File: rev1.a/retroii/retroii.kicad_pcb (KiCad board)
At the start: 4 copper layers, 362 x 215.9 mm, 294 parts, among them CON1 SD_Card_SPI, J1 VGA, J10 BARREL_JACK, J11 Conn_02x10, J12 Peripheral Slot 0, J13 74LS74, J14 Game_IO_Socket, J15 Peripheral Slot 4, J16 Peripheral Slot 1, J17 Peripheral Slot 5, J18 Peripheral Slot 2, J19 Peripheral Slot 6, J2 DB9_Female_Stacked, J20 Peripheral Slot 3, J21 Peripheral Slot 7, J22 Conn_01x09, J23 Conn_01x02, J24 Headphone, J3 DB15_Female_Stacked, J6 Edge mounted connector, J7 Cassette In, J8 Cassette Out, J9 Speaker Jack, K1 PS2_KEYBOARD, K13 LM741, P1 PROP_PLUG, P2 PROP_PLUG, Q4 MPSA13, Q5 2N3904, SW1 SW_PUSH_SAFE, SW2 SPST2, SW3 SAVE, SW4 LOAD, SW5 SW_PUSH_SAFE, SW6 RESET, SW7 MISC1, SW8 MISC2, U1 74LS00, U10 74LS08, U11 LM2576-12, U12 LM2576-5, U13 LM2576-12, U14 LM2576-3.3, U15 LM2576-5, U16 Prop_P8X32A, U17 24LC256_EEPROM, U18 74LS04, U3 74LS11, U4 Prop_P8X32A, U5 24LC256_EEPROM, U6 AT28C256_EEPROM, U8 IDT7008_Dual_Port_RAM, U9 74LS32, Y1 5MHz 20pf, Y2 ECS-2100X-1MHZ, Y3 5MHz 20pf

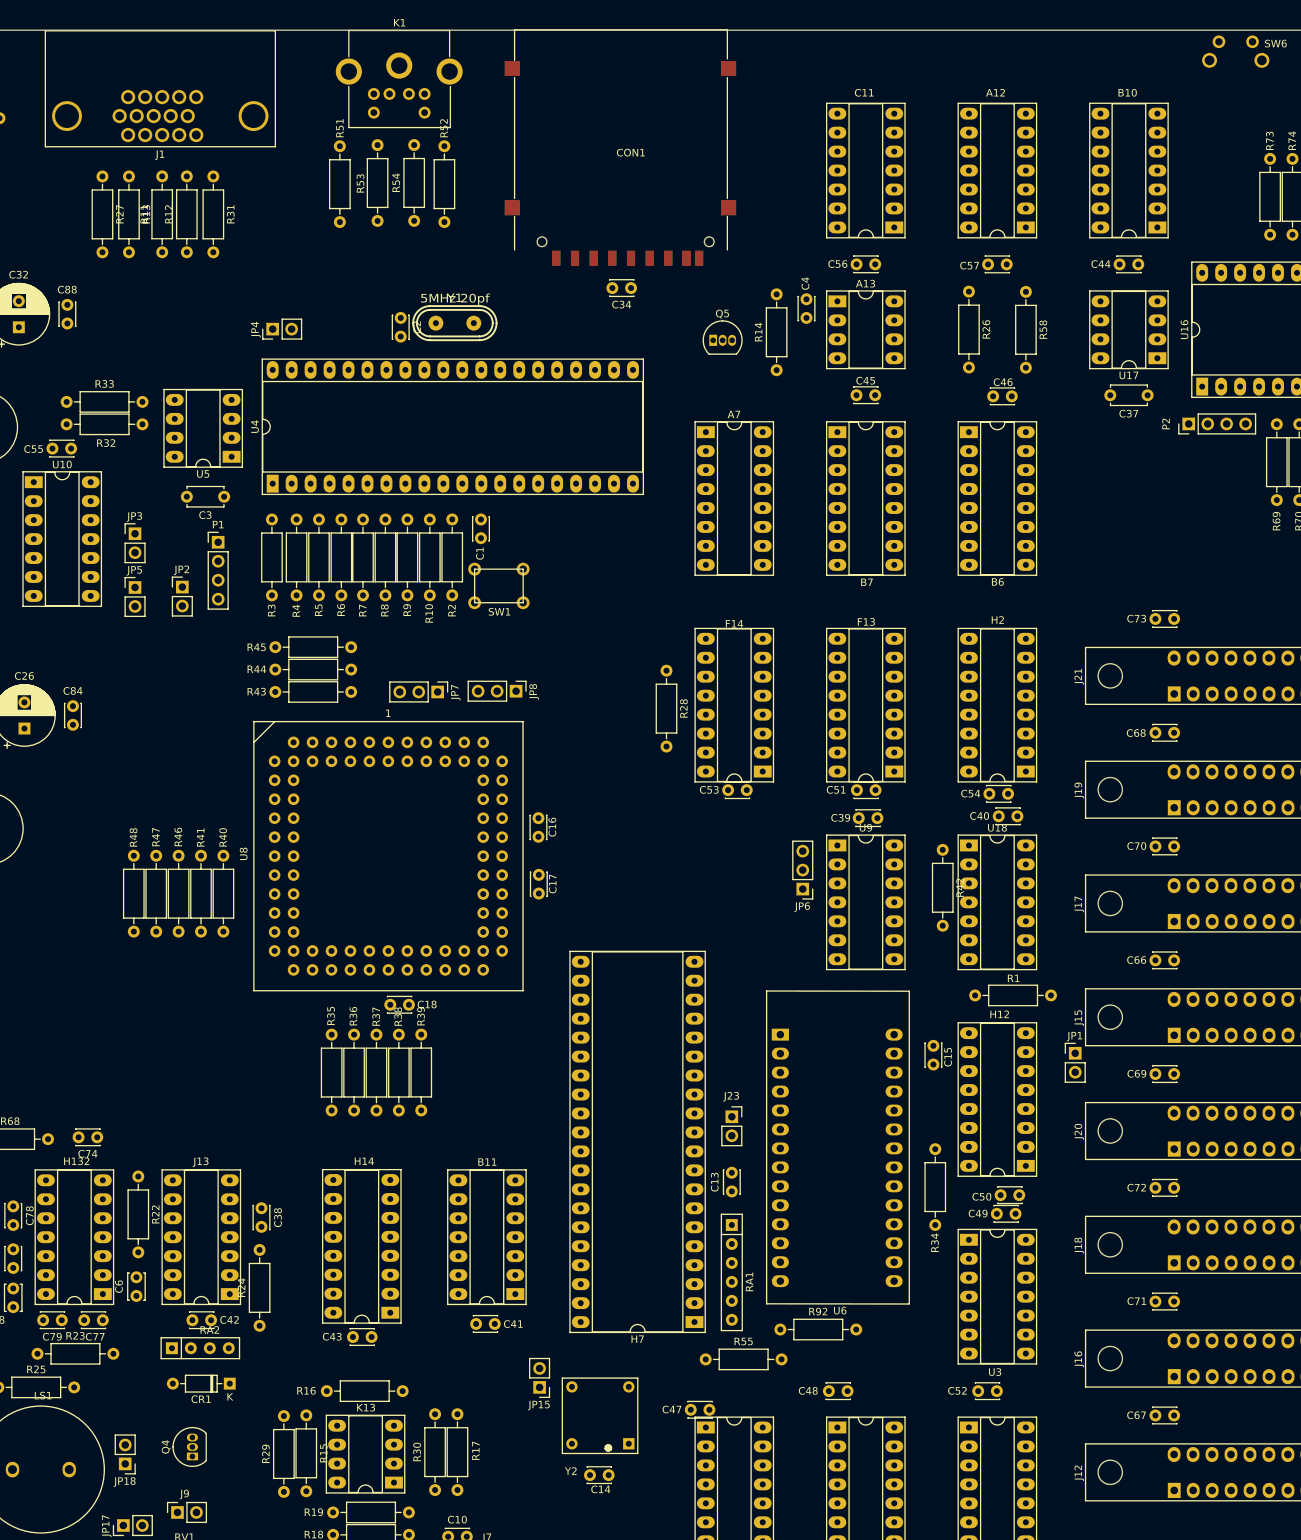
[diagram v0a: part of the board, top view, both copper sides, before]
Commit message: more keyboard circuit layout changes
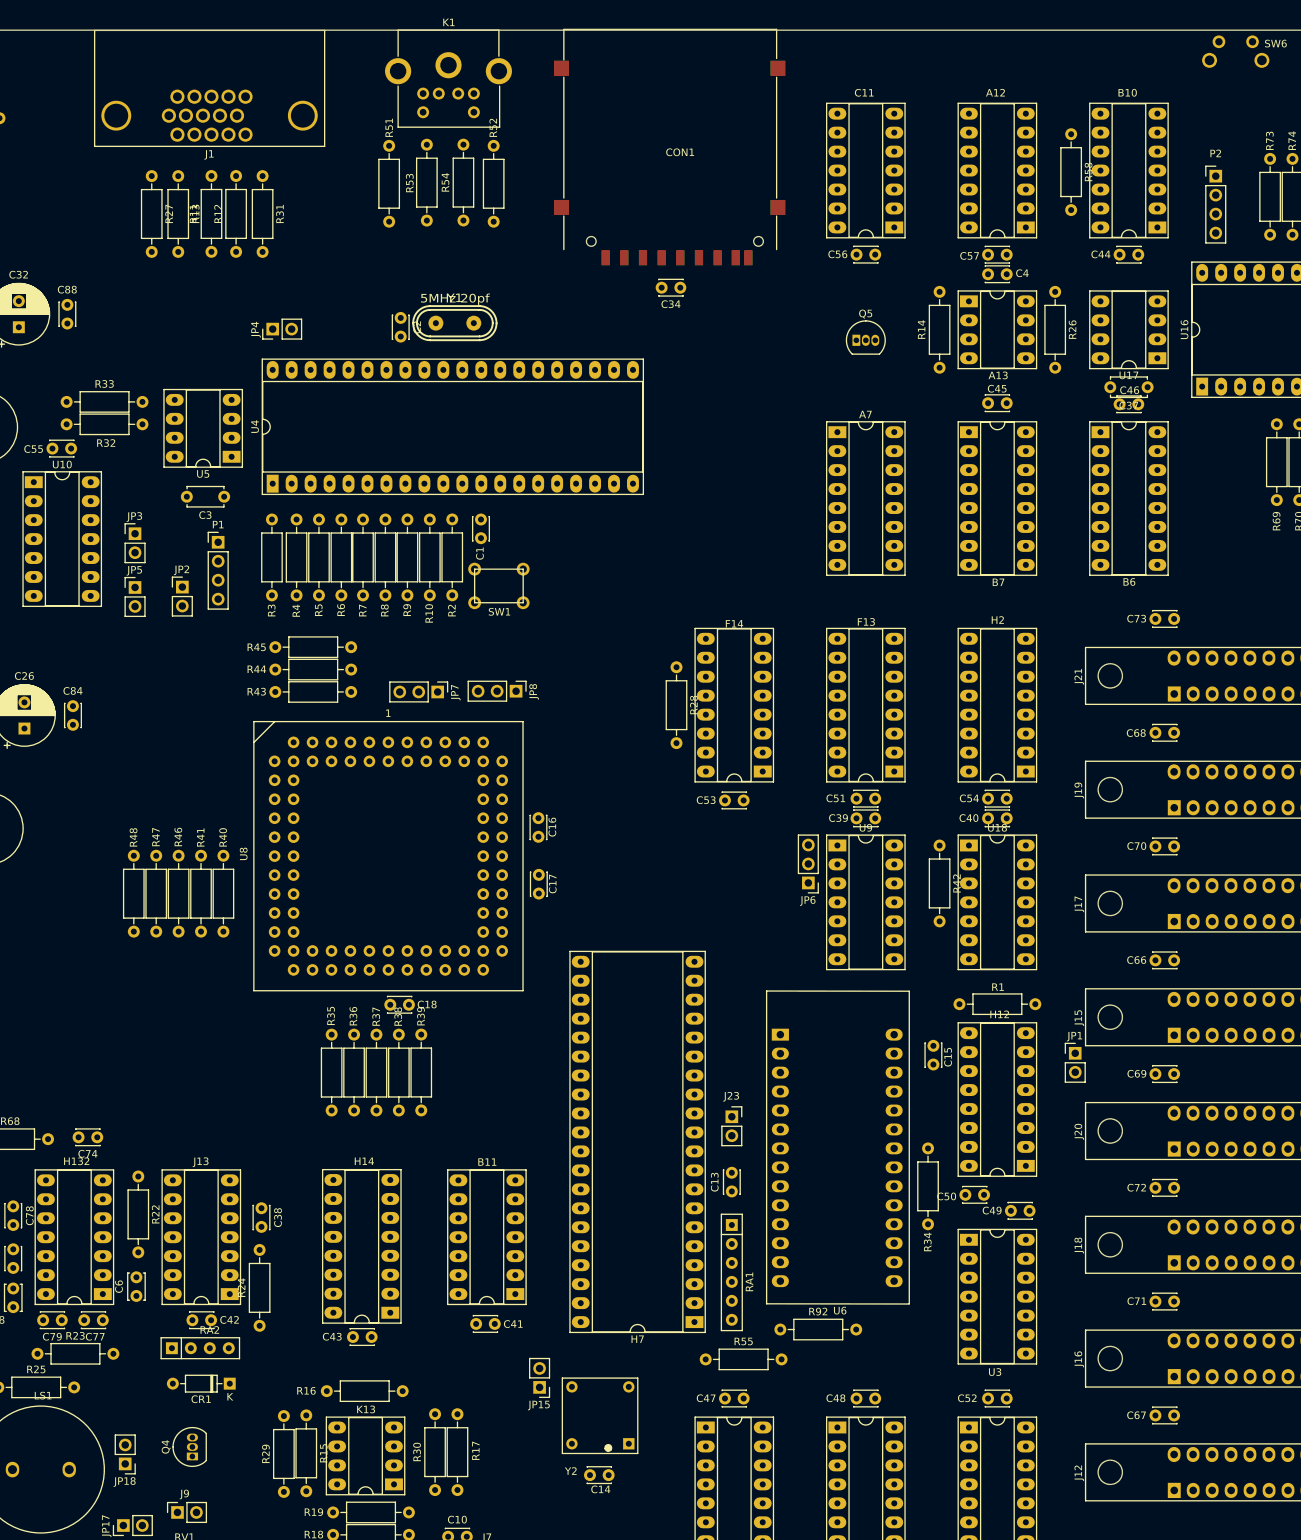
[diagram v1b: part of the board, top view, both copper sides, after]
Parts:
- moved P2 33.4 mm to (488.8, 169.5), turned to 0 degrees
- moved C4 25.0 mm to (458.3, 182.7), turned to 0 degrees
- moved R58 22.0 mm to (469.4, 163.9)
- moved R14 21.8 mm to (451.8, 195.2)
- moved Q5 19.2 mm to (440.7, 191.5)
- moved C45 17.7 mm to (460.8, 199.9)
- moved A13 17.6 mm to (455.8, 186.3)
- moved A7 17.6 mm to (438.1, 203.8)
- moved B6 17.6 mm to (473.4, 203.8)
- moved B7 17.6 mm to (455.8, 203.8)
- moved C46 17.0 mm to (478.4, 200.1)
- moved R26 11.6 mm to (467.3, 185.0)
- moved C34 6.60 mm to (417.1, 184.4)
- moved CON1 6.60 mm to (417.1, 180.4)
- moved J1 6.60 mm to (371.1, 158.4)
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
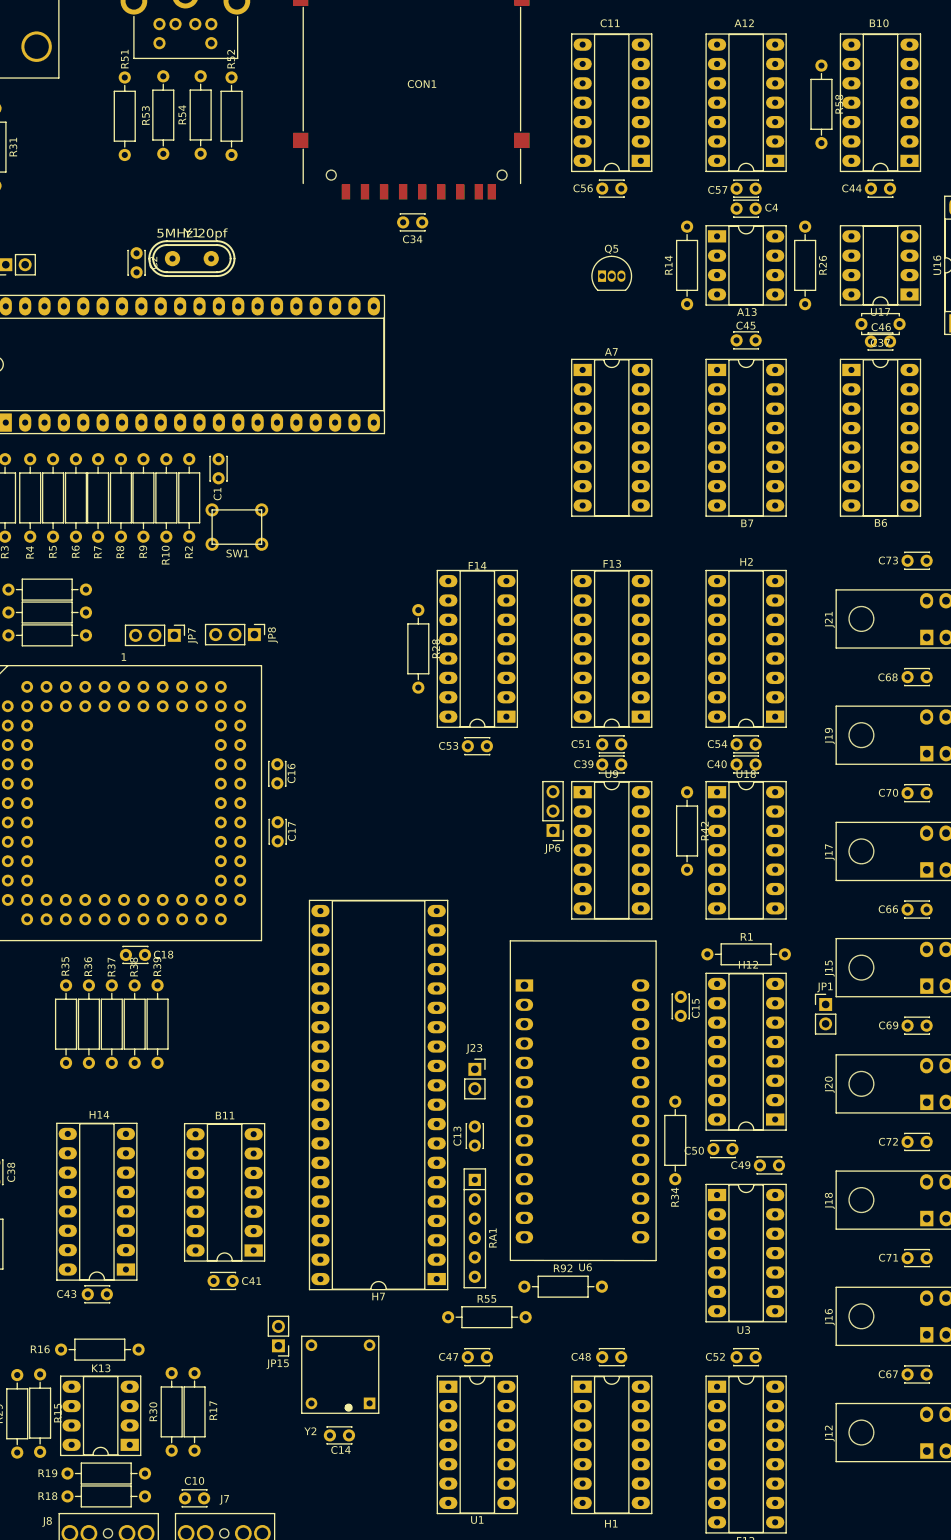
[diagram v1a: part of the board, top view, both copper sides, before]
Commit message: more general layout (address decoding, timing, keyboard)
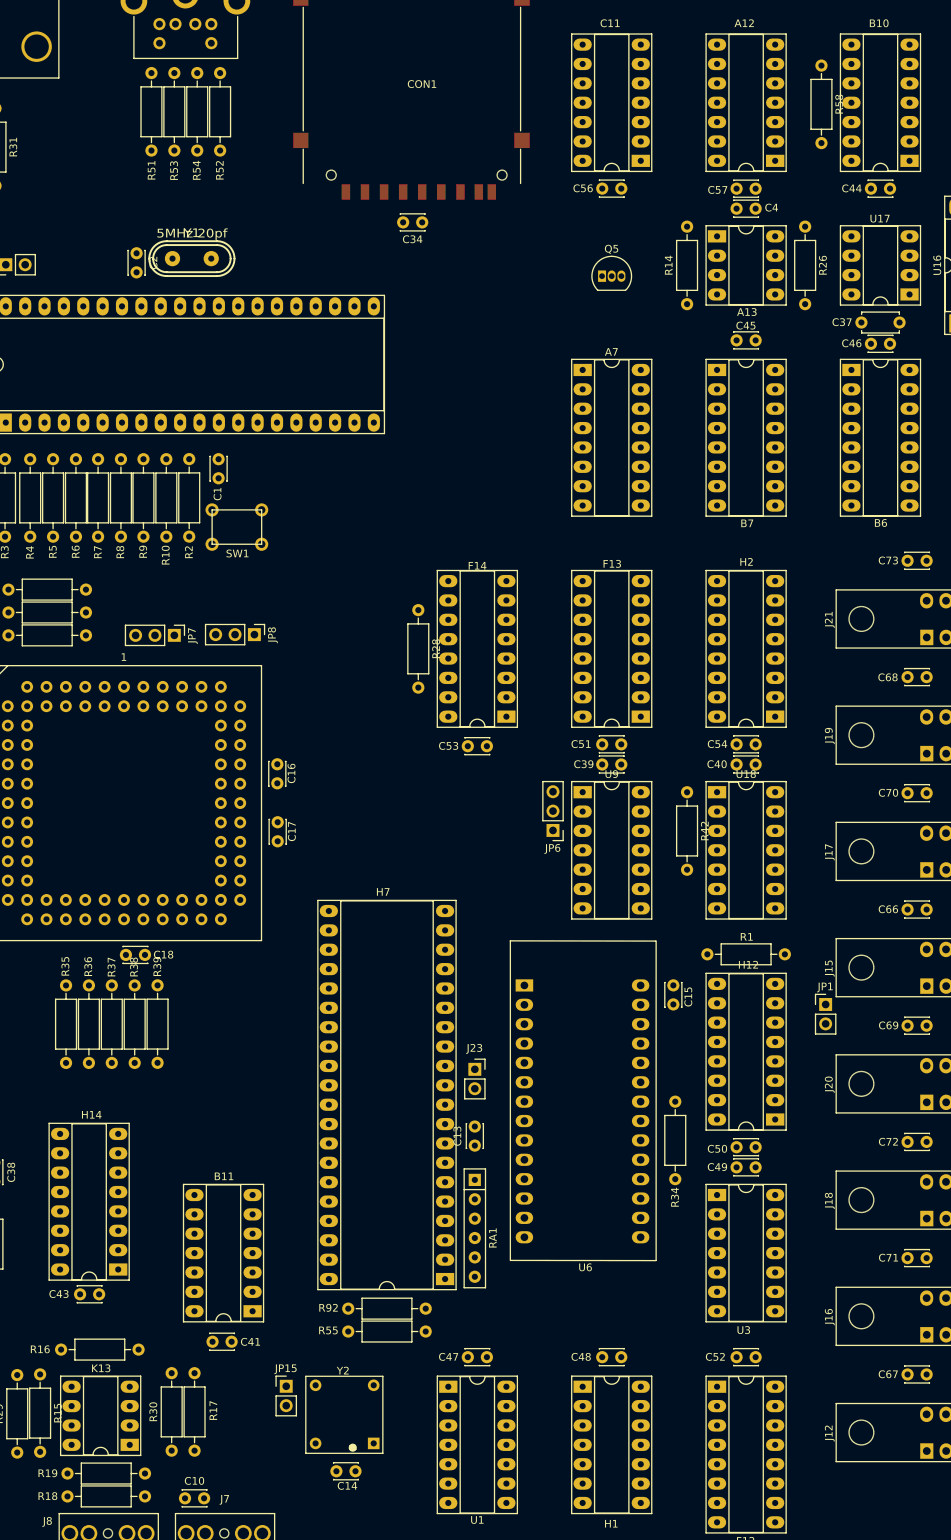
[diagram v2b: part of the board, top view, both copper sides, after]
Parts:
- moved R92 23.3 mm to (407.4, 326.9)
- moved B11 7.97 mm to (394.9, 327.2)
- moved C41 7.97 mm to (389.6, 331.2)
- moved JP15 5.41 mm to (399.3, 337.1), turned to 0 degrees
- moved Y2 5.28 mm to (407.0, 340.8)
- moved C14 4.78 mm to (405.9, 348.2)
- moved R51 3.55 mm to (381.6, 164.9)
- moved R55 3.49 mm to (417.6, 329.9), turned to 180 degrees
- moved C49 3.07 mm to (460.8, 308.4)
- moved C50 3.05 mm to (458.3, 305.7)
- moved C15 1.79 mm to (450.0, 287.0)
- moved R52 1.61 mm to (390.6, 164.9)
- moved R53 1.51 mm to (384.6, 164.9)
- moved H7 1.10 mm to (420.1, 323.0)
- moved C43 1.01 mm to (374.7, 325.0)
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
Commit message: laying out audio/serial io
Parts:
- moved R20 52.3 mm to (363.3, 311.4), turned to 270 degrees
- moved R21 52.2 mm to (346.9, 311.6), turned to 270 degrees
- moved C42 49.6 mm to (359.1, 372.1)
- moved CR1 49.6 mm to (361.6, 380.6)
- moved RA2 49.6 mm to (353.9, 375.8)
- moved R23 43.6 mm to (346.9, 286.6), turned to 270 degrees
- moved C8 42.0 mm to (363.2, 324.5), turned to 270 degrees
- moved C75 39.9 mm to (366.0, 326.9)
- moved C9 39.7 mm to (356.6, 330.9)
- moved C76 38.2 mm to (347.6, 325.3)
- moved C77 37.1 mm to (368.1, 302.1), turned to 90 degrees
- moved H131 36.6 mm to (359.0, 327.2)
- moved U10 34.0 mm to (359.0, 229.0), turned to 180 degrees
- moved C5 32.2 mm to (343.0, 328.0)
- moved C79 28.0 mm to (356.5, 305.7)
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
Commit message: more layout
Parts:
- moved RA2 70.3 mm to (369.2, 307.2)
- moved JP3 62.1 mm to (371.6, 183.9)
- moved P1 59.5 mm to (368.0, 178.8)
- moved R68 58.4 mm to (382.8, 286.2), turned to 270 degrees
- moved JP2 58.3 mm to (364.4, 186.4), turned to 180 degrees
- moved CR1 57.3 mm to (379.5, 326.1), turned to 90 degrees
- moved C74 53.5 mm to (382.8, 302.1), turned to 90 degrees
- moved C42 44.4 mm to (373.7, 330.1)
- moved JP5 36.9 mm to (375.9, 231.1)
- moved R33 13.3 mm to (347.2, 204.8), turned to 90 degrees
- moved J6 12.1 mm to (296.2, 311.9)
- moved J14 11.6 mm to (306.1, 312.0)
- moved R32 9.53 mm to (344.2, 204.8), turned to 90 degrees
- moved J11 8.87 mm to (315.5, 297.6)
- moved R35 5.10 mm to (366.8, 280.9)
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
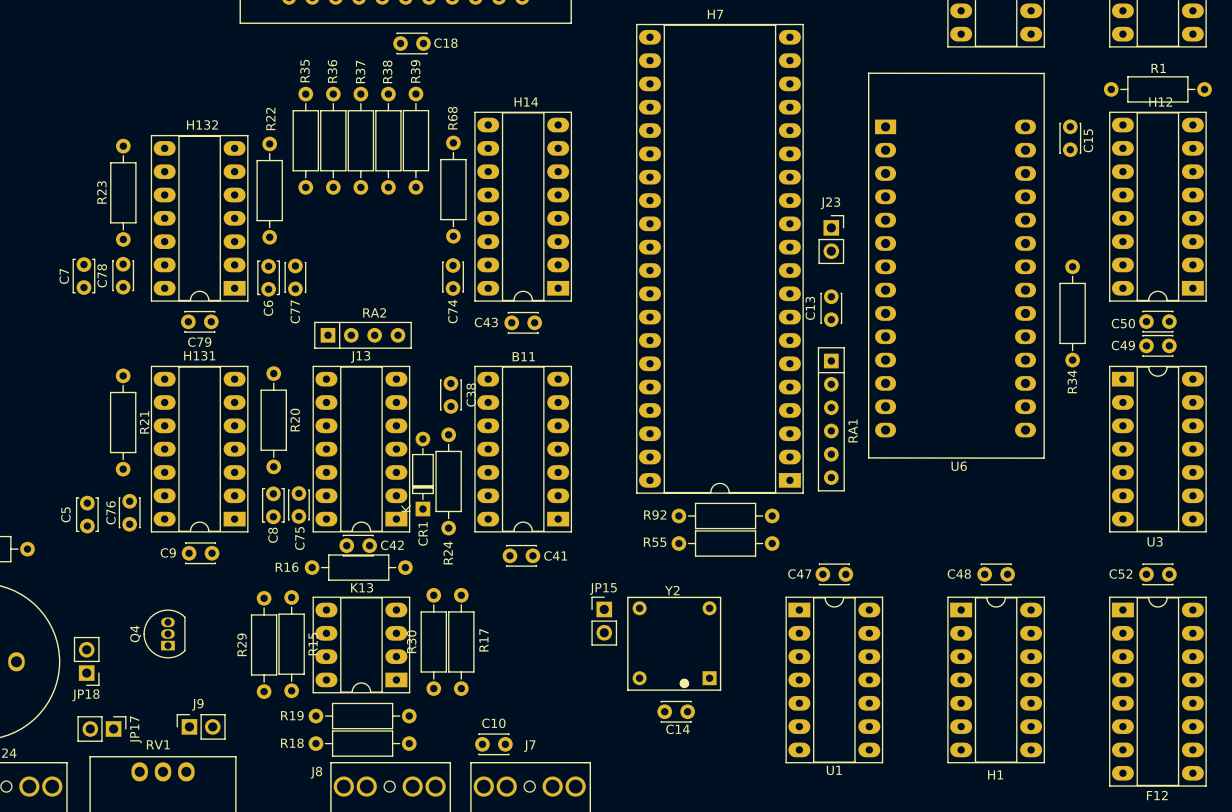
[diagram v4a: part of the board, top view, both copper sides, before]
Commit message: layout for audio/cassette in/out and serial
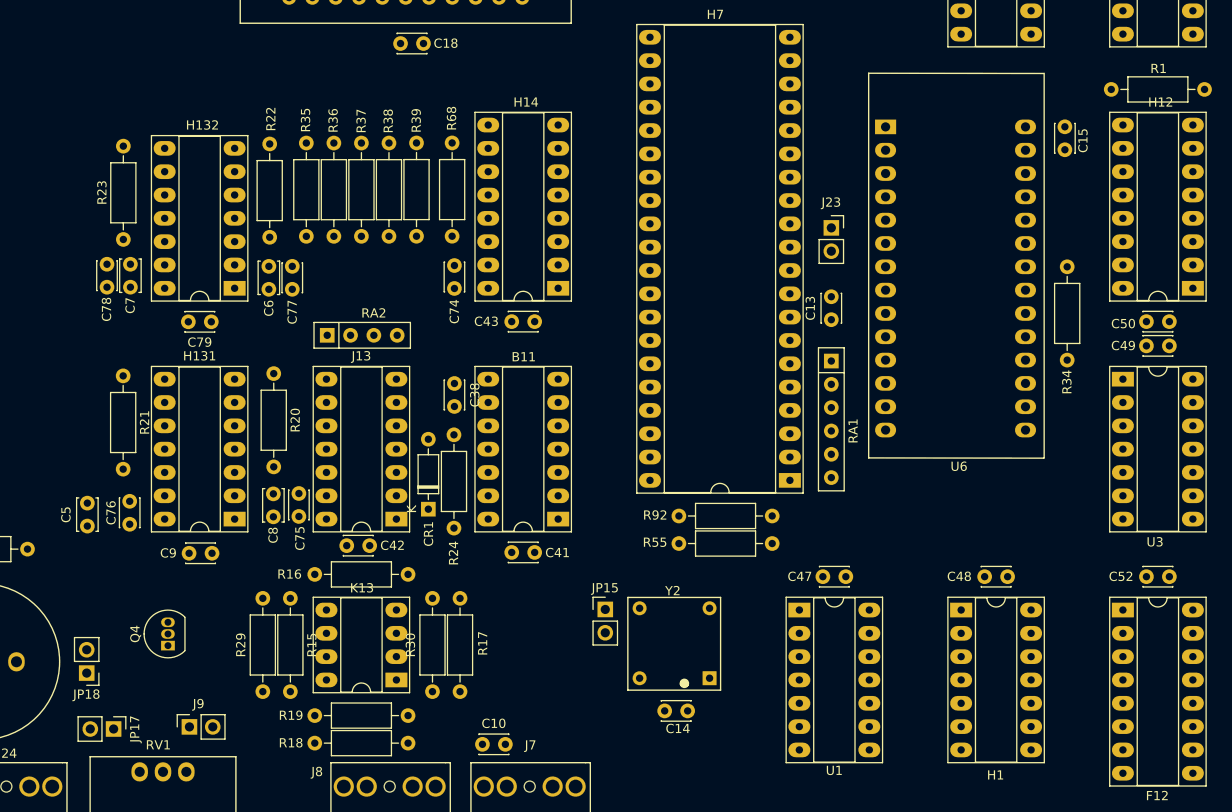
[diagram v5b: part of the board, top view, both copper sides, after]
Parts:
- moved R39 5.33 mm to (378.8, 296.4)
- moved R35 5.33 mm to (366.8, 286.3)
- moved R36 5.33 mm to (369.8, 286.3)
- moved R37 5.33 mm to (372.8, 286.3)
- moved R38 5.33 mm to (375.8, 286.3)
- moved C7 5.06 mm to (347.7, 299.5)
- moved C78 1.76 mm to (345.1, 302.0)
- moved R16 0.79 mm to (367.7, 333.2)
- moved CR1 0.59 mm to (380.1, 326.1)
- moved C15 0.59 mm to (449.4, 287.0)
- moved R34 0.59 mm to (449.7, 309.9)
- moved R24 0.58 mm to (382.9, 328.2)
- moved C41 0.42 mm to (389.2, 330.9)
- moved C38 0.38 mm to (382.9, 312.4)
- moved R17 0.36 mm to (383.6, 346.0)
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
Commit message: more layout changes on camping trip!
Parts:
- moved C55 33.9 mm to (356.4, 232.6)
- moved P1 20.8 mm to (351.4, 191.4), turned to 90 degrees
- moved R31 13.1 mm to (348.1, 169.1)
- moved JP12 5.97 mm to (255.8, 344.0)
- moved JP14 5.84 mm to (263.0, 344.0)
- moved JP13 5.78 mm to (259.4, 344.0)
- moved JP9 5.55 mm to (293.4, 344.0)
- moved JP11 5.32 mm to (300.6, 344.0)
- moved JP10 5.29 mm to (297.0, 344.0)
- moved R27 4.76 mm to (351.1, 169.1)
- moved R13 4.22 mm to (354.1, 169.1)
- moved JP2 3.65 mm to (368.0, 186.4)
- moved JP4 3.65 mm to (364.4, 186.4)
- moved R11 2.77 mm to (357.1, 179.3)
- moved JP1 2.74 mm to (467.3, 286.8)
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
